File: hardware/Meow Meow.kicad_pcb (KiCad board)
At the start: 2 copper layers, 93 x 57.5 mm, 43 parts, among them J3 SWD, P1 SPACE, P10 A, P11 W, P12 KEY_UP_ARROW, P2 KEY_DOWN_ARROW, P3 KEY_RIGHT_ARROW, P5 KEY_LEFT_ARROW, P6 D, P7 S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

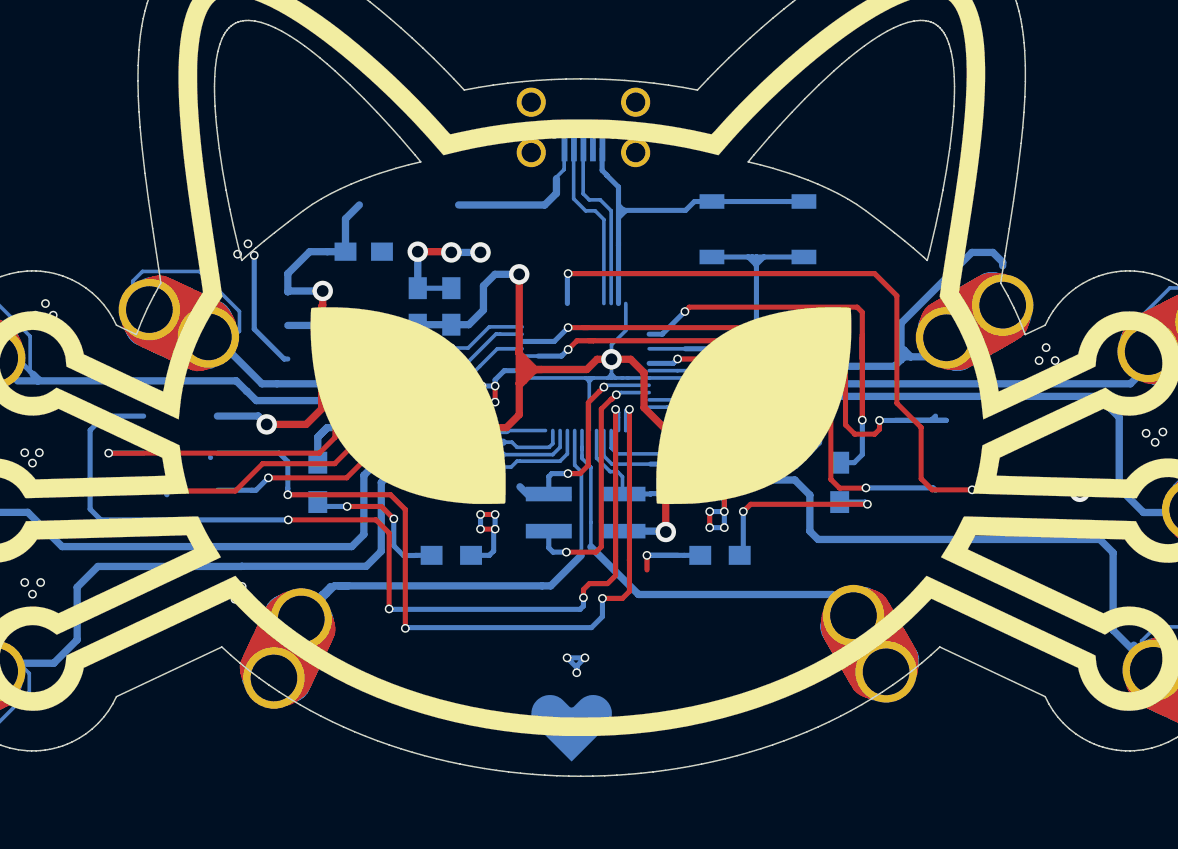
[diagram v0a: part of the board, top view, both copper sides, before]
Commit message: Update pcb to SAMD11
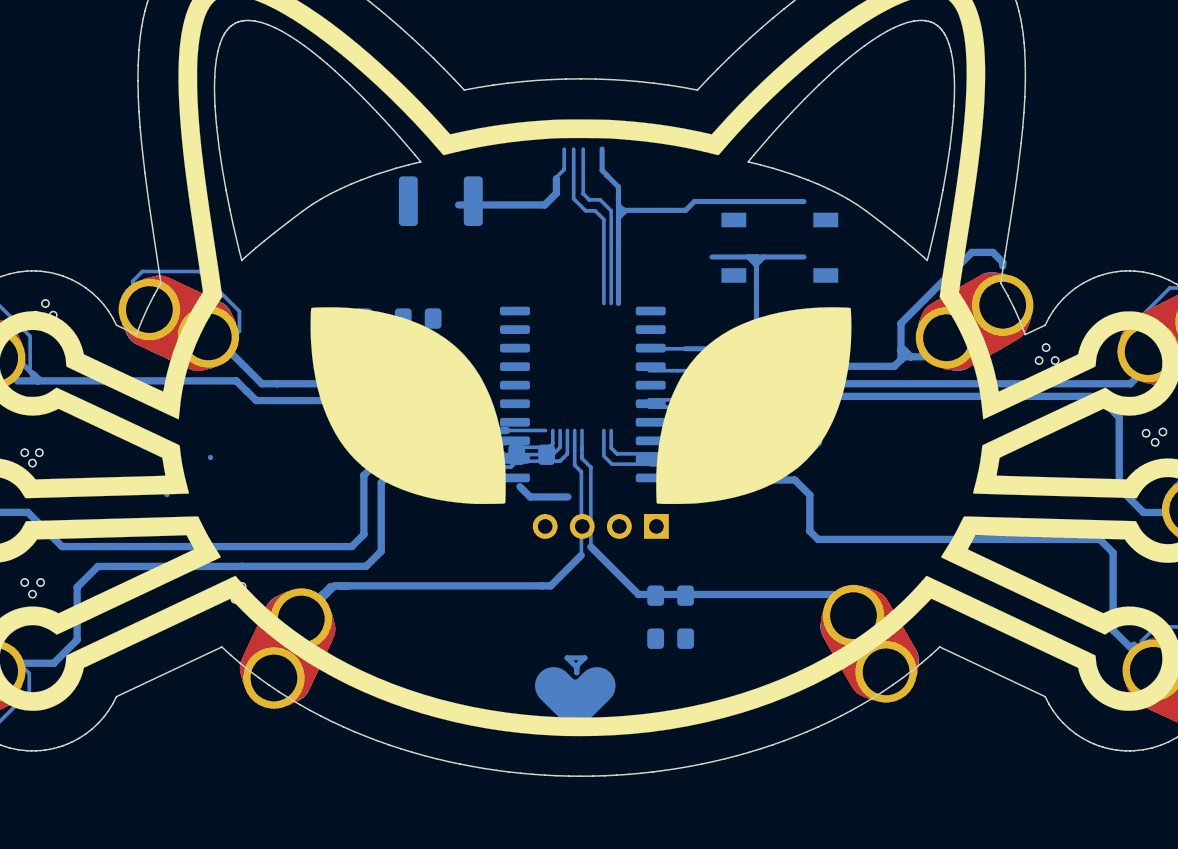
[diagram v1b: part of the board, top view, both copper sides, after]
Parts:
- removed C1: 1uF, Capacitors_SMD:C_0805_HandSoldering
- removed P9: USB_Micro, Connectors:U254051N4BH806
- added F1: 0.5A, Resistor_SMD:R_1812_4532Metric_Pad1.30x3.40mm_HandSolder, B.Cu at (133.3, 99.7)
- added R1: 10K, Resistor_SMD:R_0805_2012Metric_Pad1.15x1.40mm_HandSolder, B.Cu at (152.4, 111.0)
- added U1: ATSAMD11D14A-SS, Package_SO:SOIC-20W_7.5x12.8mm_P1.27mm, B.Cu at (143.0, 113.0)
- added U2: AP2112K-3.3, Package_TO_SOT_SMD:SOT-23-5, B.Cu at (152.4, 114.8)
- C2, C4, C5, C6: footprint Capacitors_SMD:C_0805_HandSoldering -> Capacitor_SMD:C_0805_2012Metric_Pad1.15x1.40mm_HandSolder
- D1, D2: footprint LEDs:LED_0805_HandSoldering -> LED_SMD:LED_0805_2012Metric_Pad1.15x1.40mm_HandSolder
- J3: footprint Pin_Headers:Pin_Header_Straight_2x02_Pitch2.54mm_SMD -> Connector_PinSocket_2.54mm:PinSocket_1x04_P2.54mm_Vertical
- R2, R3: footprint Resistors_SMD:R_0805_HandSoldering -> Resistor_SMD:R_0805_2012Metric_Pad1.15x1.40mm_HandSolder
- SW1: value SW_Push -> RESET; footprint Buttons_Switches_SMD:SW_SPST_TL3342 -> Button_Switch_SMD:SW_SPST_TL3342
- moved C6 26.4 mm to (157.0, 114.4), turned to 0 degrees
- moved R3 26.3 mm to (131.7, 107.8), turned to 0 degrees
- moved D2 25.9 mm to (134.8, 117.7), turned to 0 degrees
- moved C5 24.9 mm to (149.0, 126.8), turned to 0 degrees
- moved C4 18.0 mm to (139.5, 117.1)
- moved R2 17.7 mm to (127.0, 107.8)
- moved C2 16.6 mm to (149.0, 129.7)
- moved G*** 8.36 mm to (116.4, 118.3)
- moved G*** 6.34 mm to (169.4, 120.2)
- moved D1 5.35 mm to (130.0, 117.4), turned to 0 degrees
- moved J3 4.94 mm to (148.1, 122.0), turned to 90 degrees
- moved SW1 1.96 mm to (156.5, 102.9), turned to 0 degrees
- moved svg2mod 1.93 mm to (142.5, 134.0)
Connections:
- D2 pad 2: /D8 -> /LED
- P1 pad 1: /Y15 -> /Y12
- P10 pad 1: /Y9 -> /Y7
- P11 pad 1: /Y8 -> /Y6
- P8 pad 1: /Y14 -> /Y10
- SW1 pad 2: Net-(SW1-Pad2) -> /RST
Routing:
- net +3V3: track 100.0 -> 0.00 mm, vias 4 -> 0
- net GND: track 107.9 -> 29.3 mm, vias 43 -> 18
- net /SCL: track 65.9 -> 0.00 mm, vias 4 -> 0
- net /SDA: track 56.5 -> 0.01 mm, vias 4 -> 0
- net /I2S_D1/X7: track 44.8 -> 0.00 mm, vias 2 -> 0
- net /CS: track 43.7 -> 0.00 mm, vias 2 -> 0
- net /I2S_SCK: track 38.9 -> 0.00 mm, vias 2 -> 0
- net /MOSI: track 38.0 -> 0.03 mm, vias 2 -> 0
- net /SCK: track 37.1 -> 0.00 mm, vias 2 -> 0
- net /D8: track 34.3 -> 0.00 mm, vias 2 -> 0
- net /MISO: track 27.8 -> 0.00 mm, vias 2 -> 0
- net VCC: track 27.8 -> 0.00 mm, vias 2 -> 0
- net Net-(SW1-Pad2): track 21.9 -> 0.00 mm
- net Net-(D2-Pad1): track 13.8 -> 0.00 mm, vias 2 -> 0
- net /SWCLK: track 16.4 -> 3.57 mm, vias 2 -> 0
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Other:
- board text added: "Meow Meow Mini"
- board text added: "v 1.0"
- board text removed: "Meow Meow"
- board text removed: "v 1.3"

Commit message: Update size
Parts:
- removed the G*** at (142.9, 101.6)
- removed the G*** at (142.7, 129.0)
- moved G*** 48.4 mm to (124.1, 137.2)
- moved C2 19.0 mm to (161.7, 115.6)
- moved G*** 18.6 mm to (115.6, 136.9)
- moved P6 16.3 mm to (170.4, 124.2)
- moved P5 15.4 mm to (113.4, 124.5)
- moved P3 15.0 mm to (112.2, 117.1)
- moved P7 14.3 mm to (173.4, 116.6)
- moved P2 14.3 mm to (115.1, 109.4)
- moved C5 13.3 mm to (159.3, 118.3)
- moved P10 12.7 mm to (171.2, 109.0)
- moved D2 11.6 mm to (124.8, 111.8)
- moved P1 10.4 mm to (128.9, 121.7)
- moved P8 10.2 mm to (155.6, 122.9)
- moved P11 9.54 mm to (160.7, 105.0)
- moved P12 8.88 mm to (124.2, 106.5)
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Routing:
- net /Y2: track 67.3 -> 0.00 mm
- net /Y3: track 66.9 -> 0.00 mm
- net /Y0: track 66.2 -> 0.00 mm
- net /Y1: track 64.1 -> 4.81 mm
- net /Y4: track 57.4 -> 0.00 mm
- net /Y9: track 54.5 -> 0.00 mm
- net /Y5: track 40.2 -> 0.00 mm
- net /Y8: track 37.0 -> 0.00 mm
- net /Y15: track 34.5 -> 0.15 mm
- net GND: track 29.3 -> 0.00 mm, vias 18 -> 0
- net /Y14: track 28.1 -> 0.00 mm
- net /SWDIO: track 21.9 -> 0.00 mm
- net /D-: track 16.6 -> 0.00 mm
- net /D+: track 11.8 -> 0.00 mm
- net Net-(F1-Pad2): track 10.5 -> 0.00 mm
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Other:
- board size 93 x 57.5 mm -> 73.1 x 45.2 mm
- board text removed: "X3"
- board text removed: "X7"

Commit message: add library and layout
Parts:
- removed C5: 0.1uF, Capacitor_SMD:C_0805_2012Metric_Pad1.15x1.40mm_HandSolder
- removed J3: SWD, Connector_PinSocket_2.54mm:PinSocket_1x04_P2.54mm_Vertical
- removed R1: 10K, Resistor_SMD:R_0805_2012Metric_Pad1.15x1.40mm_HandSolder
- added J1: USB_B_Micro, Connectors:U254051N4BH806, B.Cu at (142.8, 97.4)
- added J2: SWD, Connector_PinHeader_2.54mm:PinHeader_1x04_P2.54mm_Vertical, B.Cu at (138.9, 128.4)
- P8: footprint Connectors_EC:SEWALLI_renew -> MeowMeow:SEWALLI_renew
- moved G*** 41.1 mm to (88.0, 110.2)
- moved R2 32.3 mm to (160.8, 120.2), turned to 270 degrees
- moved G*** 30.7 mm to (180.3, 139.1)
- moved G*** 30.1 mm to (188.6, 112.0)
- moved D1 30.0 mm to (163.0, 120.2), turned to 270 degrees
- moved F1 22.8 mm to (155.2, 101.7), turned to 330 degrees
- moved C4 22.7 mm to (154.5, 104.9), turned to 150 degrees
- moved SW1 21.5 mm to (131.7, 102.8), turned to 30 degrees
- moved G*** 21.1 mm to (106.1, 136.8)
- moved C2 19.5 mm to (144.6, 106.3), turned to 180 degrees
- moved C6 16.0 mm to (144.6, 104.4), turned to 180 degrees
- moved G*** 13.5 mm to (164.2, 136.9)
- moved U2 9.68 mm to (149.0, 105.7), turned to 180 degrees
- moved D2 8.82 mm to (122.0, 120.2), turned to 270 degrees
- moved R3 7.31 mm to (124.3, 120.2), turned to 270 degrees
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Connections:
- F1 pad 1: VCC -> Net-(F1-Pad1)
- F1 pad 2: Net-(F1-Pad2) -> VCC
- U1 pad 1: /Y3 -> /Y1
- U1 pad 10: /Y13 -> /Y2
- U1 pad 19: /Y1 -> /Y7
- U1 pad 2: /Y4 -> /Y10
- U1 pad 20: /Y2 -> /Y6
- U1 pad 3: /Y5 -> /Y12
- U1 pad 6: /Y6 -> /Y5
- U1 pad 7: /Y7 -> /Y4
- U1 pad 8: /Y10 -> /Y13
- U1 pad 9: /Y12 -> /Y3
- U2 pad 3: Net-(R1-Pad2) -> VCC
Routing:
- net +3V3: track 0.00 -> 63.9 mm, vias 0 -> 3
- net /Y0: track 0.00 -> 45.2 mm
- net /Y4: track 0.00 -> 43.9 mm
- net /Y3: track 0.00 -> 42.3 mm
- net /Y2: track 0.00 -> 41.9 mm
- net /Y7: track 0.00 -> 39.3 mm
- net /LED: track 0.00 -> 39.1 mm, vias 0 -> 2
- net /Y1: track 4.81 -> 43.6 mm
- net /Y12: track 0.00 -> 36.9 mm
- net /Y5: track 0.00 -> 35.5 mm
- net /SWCLK: track 0.00 -> 27.2 mm, vias 0 -> 2
- net /SWDIO: track 0.00 -> 27.0 mm, vias 0 -> 2
- net /Y10: track 0.00 -> 25.9 mm
- net GND: track 0.00 -> 25.9 mm, vias 0 -> 12
- net /Y6: track 0.00 -> 24.5 mm
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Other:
- net class Default: clearance 0.2 -> 0.001
- net class vcc: via_dia 1.4 -> 1; via_drill 0.8 -> 0.6
- rule trace_clearance: 0.2 -> 0.001

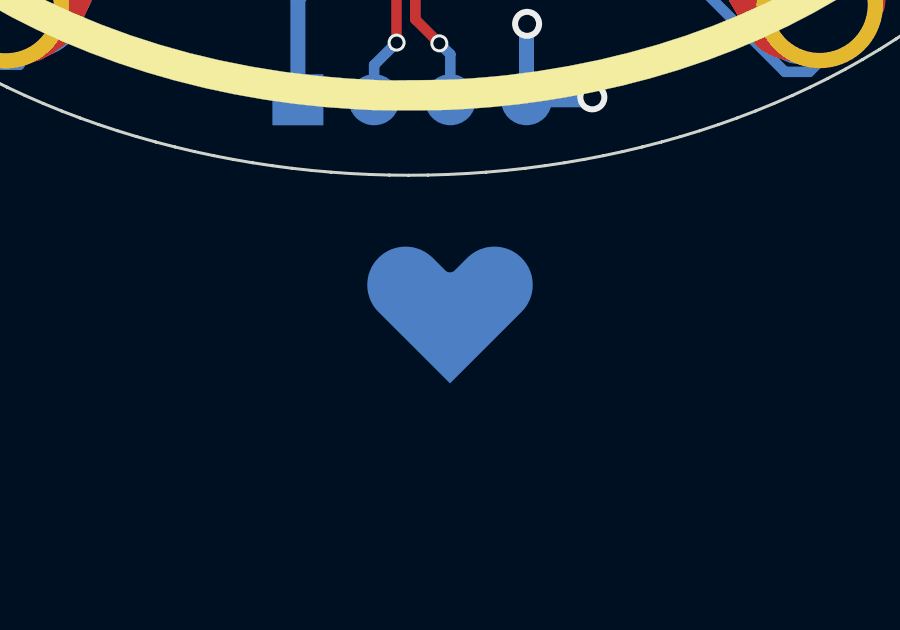
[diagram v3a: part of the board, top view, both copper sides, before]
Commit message: update logos
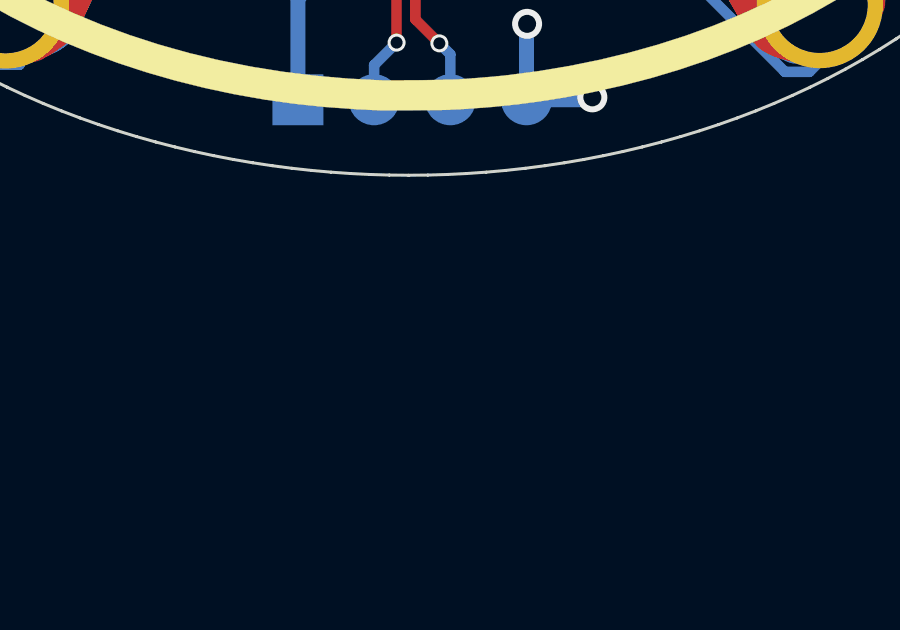
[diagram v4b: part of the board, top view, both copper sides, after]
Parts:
- removed the G*** at (88.0, 110.2)
- removed the G*** at (180.3, 139.1)
- removed the G*** at (115.6, 136.9)
- removed the svg2mod at (143.9, 135.7)
- added G***: LOGO, Aesthetics:led, B.Cu at (123.2, 116.3)
- added Ref**: Val**, Aesthetics:heart, F.Cu at (142.7, 124.2)
- moved G*** 50.5 mm to (138.4, 105.7)
- moved G*** 40.5 mm to (157.7, 114.6)
- moved G*** 32.7 mm to (132.6, 117.6)
- moved G*** 22.9 mm to (151.9, 117.6)
- moved G*** 15.8 mm to (129.5, 109.7)
- moved G*** 14.1 mm to (119.4, 123.2)
- moved G*** 13.9 mm to (166.9, 122.2)
- moved G*** 13.4 mm to (117.6, 116.3)
- moved G*** 13.0 mm to (168.1, 116.3)
- moved REF*** 12.8 mm to (120.9, 94.0)
- moved G*** 11.4 mm to (118.4, 111.5)
- moved G*** 10.7 mm to (166.9, 111.0)
- moved G*** 8.17 mm to (155.7, 108.2)
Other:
- board text added: "electroniccats.com"
- board text removed: "3v3"
- board text removed: "CLK"
- board text removed: "DIO"
- board text removed: "GND"
- board text removed: "ON"
- board text removed: "electroniccats.com/howtomeow"
